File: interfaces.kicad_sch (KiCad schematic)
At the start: 23 parts, among them J3 SI-51005-F

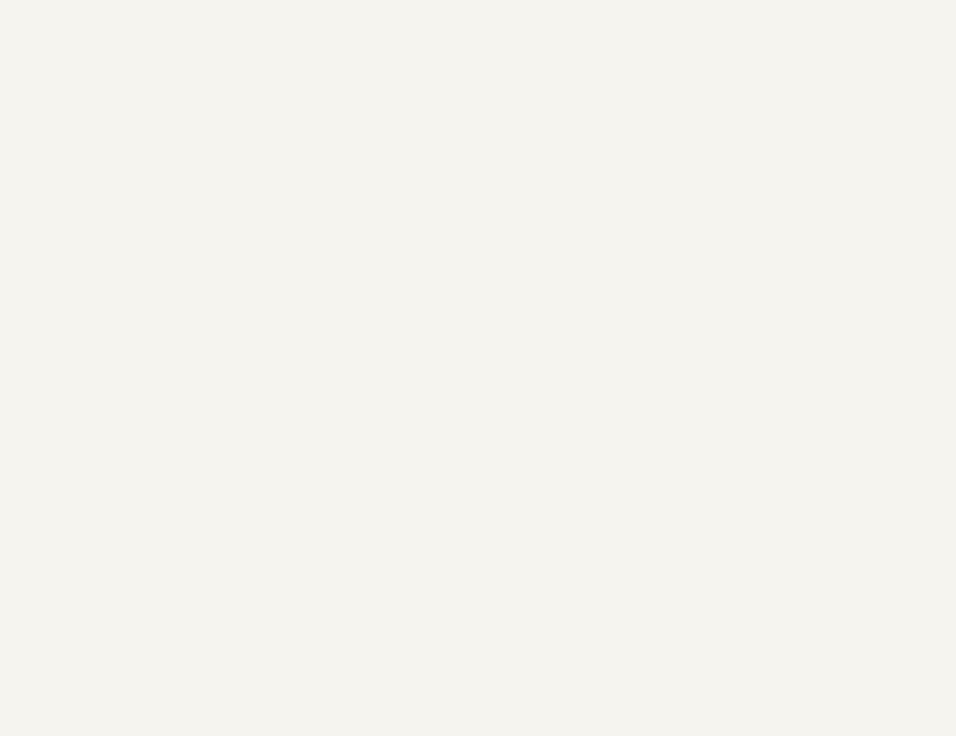
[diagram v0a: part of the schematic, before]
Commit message: Added I2C connector
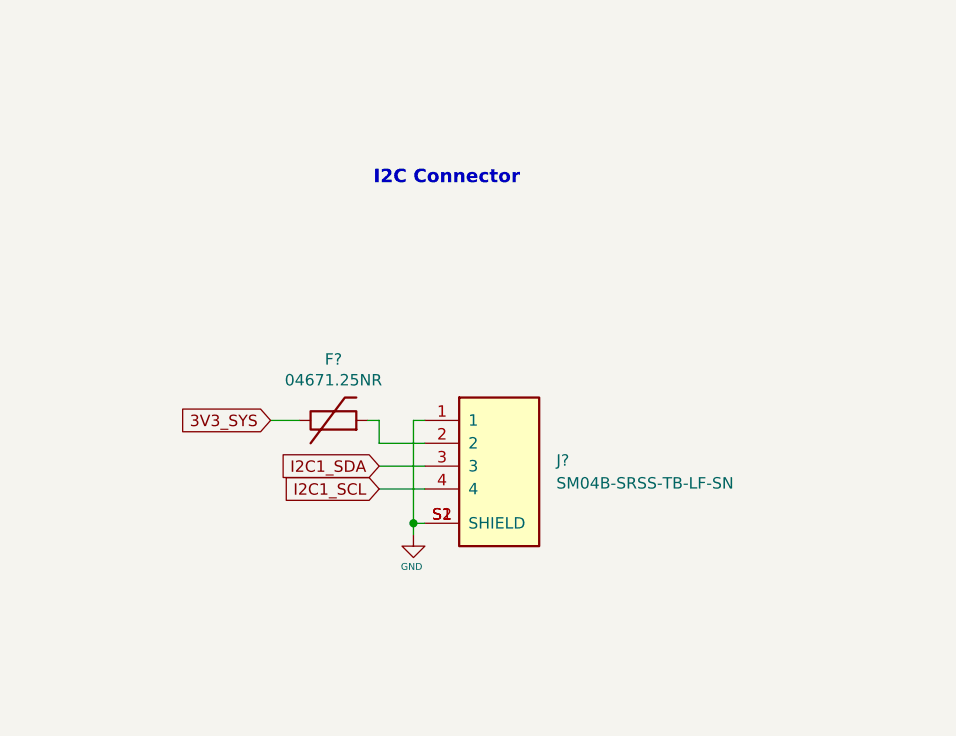
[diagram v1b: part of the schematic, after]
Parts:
- added F?: 04671.25NR, jetson-nano-baseboard-footprints:0603-Fuse-Littelfuse-0467, symbol jetson-nano-baseboard:04671.25NR
- added J?: SM04B-SRSS-TB-LF-SN, jetson-nano-baseboard-footprints:SM04B-SRSS-TB-LF-SN, symbol jetson-nano-baseboard:SM04B-SRSS-TB-LF-SN
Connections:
- net 3V3_SYS: now also F?.1
- net GND: now also J?.1, J?.S1 (SHIELD), J?.S2 (SHIELD)
- new net: F?.2, J?.2
- new net I2C1_SCL: J?.4
- new net I2C1_SDA: J?.3
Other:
- note added: "I2C Connector"
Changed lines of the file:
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@@
   (junction (at 161.925 142.24) (diameter 0) (color 0 0 0 0)
   )
+  (junction (at 305.435 76.2) (diameter 0) (color 0 0 0 0)
+  )
   (junction (at 113.665 129.54) (diameter 0) (color 0 0 0 0)
   )
@@
     (stroke (width 0) (type default) (color 0 0 0 0))
   )
+  (wire (pts (xy 300.355 64.77) (xy 301.625 64.77))
+    (stroke (width 0) (type default) (color 0 0 0 0))
+  )
   (wire (pts (xy 159.385 203.2) (xy 161.925 203.2))
     (stroke (width 0) (type default) (color 0 0 0 0))
@@
     (stroke (width 0) (type default) (color 0 0 0 0))
   )
+  (wire (pts (xy 305.435 76.2) (xy 306.705 76.2))
+    (stroke (width 0) (type default) (color 0 0 0 0))
+  )
   (wire (pts (xy 159.385 172.72) (xy 161.925 172.72))
     (stroke (width 0) (type default) (color 0 0 0 0))
@@
     (stroke (width 0) (type default) (color 0 0 0 0))
   )
+  (wire (pts (xy 305.435 77.47) (xy 305.435 76.2))
+    (stroke (width 0) (type default) (color 0 0 0 0))
+  )
   (wire (pts (xy 91.44 120.65) (xy 91.44 131.445))
     (stroke (width 0) (type default) (color 0 0 0 0))
@@
     (stroke (width 0) (type default) (color 0 0 0 0))
   )
+  (wire (pts (xy 301.625 64.77) (xy 301.625 67.31))
+    (stroke (width 0) (type default) (color 0 0 0 0))
+  )
   (wire (pts (xy 300.355 172.72) (xy 299.085 172.72))
     (stroke (width 0) (type default) (color 0 0 0 0))
@@
     (stroke (width 0) (type default) (color 0 0 0 0))
   )
+  (wire (pts (xy 301.625 72.39) (xy 306.705 72.39))
+    (stroke (width 0) (type default) (color 0 0 0 0))
+  )
   (wire (pts (xy 90.805 184.15) (xy 90.805 182.88))
     (stroke (width 0) (type default) (color 0 0 0 0))
@@
     (stroke (width 0) (type default) (color 0 0 0 0))
   )
+  (wire (pts (xy 301.625 69.85) (xy 306.705 69.85))
+    (stroke (width 0) (type default) (color 0 0 0 0))
+  )
   (wire (pts (xy 159.385 210.82) (xy 161.925 210.82))
     (stroke (width 0) (type default) (color 0 0 0 0))
@@
     (stroke (width 0) (type default) (color 0 0 0 0))
   )
+  (wire (pts (xy 289.56 64.77) (xy 292.735 64.77))
+    (stroke (width 0) (type default) (color 0 0 0 0))
+  )
+  (wire (pts (xy 305.435 64.77) (xy 305.435 76.2))
+    (stroke (width 0) (type default) (color 0 0 0 0))
+  )
   (wire (pts (xy 161.925 203.2) (xy 161.925 210.82))
     (stroke (width 0) (type default) (color 0 0 0 0))
@@
     (stroke (width 0) (type default) (color 0 0 0 0))
   )
+  (wire (pts (xy 301.625 67.31) (xy 306.705 67.31))
+    (stroke (width 0) (type default) (color 0 0 0 0))
+  )
   (wire (pts (xy 113.665 129.54) (xy 113.665 193.04))
     (stroke (width 0) (type default) (color 0 0 0 0))
   )
+  (wire (pts (xy 306.705 64.77) (xy 305.435 64.77))
+    (stroke (width 0) (type default) (color 0 0 0 0))
+  )
   (wire (pts (xy 161.925 218.44) (xy 161.925 229.235))
     (stroke (width 0) (type default) (color 0 0 0 0))
@@
     (effects (font (size 1.524 1.524)) (justify left bottom))
   )
+  (text "I2C Connector" (at 300.99 38.735 0)
+    (effects (font (size 1.4986 1.4986) (thickness 0.2997) bold) (justify left bottom))
+  )
   (text "Text" (at 67.7926 1253.8202 0)
     (effects (font (size 1.524 1.524)) (justify left bottom))
@@
     )
   )
+  (global_label "3V3_SYS" (shape input) (at 289.56 64.77 180) (fields_autoplaced)
+    (effects (font (size 1.27 1.27)) (justify right))
+    (property "Intersheet References" "${INTERSHEET_REFS}" (id 0) (at 168.91 145.415 0)
+      (effects (font (size 1.27 1.27)) hide)
+    )
+  )
   (global_label "PCIE0_TX0_P" (shape input) (at 212.09 152.4 0) (fields_autoplaced)
     (effects (font (size 1.27 1.27)) (justify left))
@@
     )
   )
+  (global_label "I2C1_SCL" (shape input) (at 301.625 72.39 180) (fields_autoplaced)
+    (effects (font (size 1.27 1.27)) (justify right))
+    (property "Intersheet References" "${INTERSHEET_REFS}" (id 0) (at 290.5318 72.3106 0)
+      (effects (font (size 1.27 1.27)) (justify right) hide)
+    )
+  )
   (global_label "1V8_SYS" (shape input) (at 101.6 120.65 90) (fields_autoplaced)
     (effects (font (size 1.27 1.27)) (justify left))
@@
     )
   )
+  (global_label "I2C1_SDA" (shape input) (at 301.625 69.85 180) (fields_autoplaced)
+    (effects (font (size 1.27 1.27)) (justify right))
+    (property "Intersheet References" "${INTERSHEET_REFS}" (id 0) (at 290.4713 69.7706 0)
+      (effects (font (size 1.27 1.27)) (justify right) hide)
+    )
+  )
   (global_label "PCIE0_RX1_P" (shape input) (at 212.09 175.26 0) (fields_autoplaced)
     (effects (font (size 1.27 1.27)) (justify left))
@@
     (pin "1")
     (pin "2")
+  )
+  (symbol (lib_id "jetson-nano-baseboard:SM04B-SRSS-TB-LF-SN") (at 311.785 71.12 0) (unit 1)
+    (in_bom yes) (on_board yes) (fields_autoplaced)
+    (property "Reference" "J?" (id 0) (at 321.31 69.2149 0)
+      (effects (font (size 1.27 1.27)) (justify left))
+    )
+    (property "Value" "SM04B-SRSS-TB-LF-SN" (id 1) (at 321.31 71.7549 0)
+      (effects (font (size 1.27 1.27)) (justify left))
+    )
+    (property "Footprint" "jetson-nano-baseboard-footprints:SM04B-SRSS-TB-LF-SN" (id 2) (at 311.785 85.09 0)
+      (effects (font (size 1.27 1.27)) hide)
+    )
+    (property "Datasheet" "https://www.jst-mfg.com/product/pdf/eng/eSH.pdf" (id 3) (at 300.355 86.36 0)
+      (effects (font (size 1.27 1.27)) hide)
+    )
+    (property "MPN" "SM04B-SRSS-TB-LF-SN" (id 4) (at 309.245 87.63 0)
+      (effects (font (size 1.27 1.27)) (justify left) hide)
+    )
+    (property "Manufacturer" "JST" (id 5) (at 309.245 90.17 0)
+      (effects (font (size 1.27 1.27)) (justify left) hide)
+    )
+    (pin "1")
+    (pin "2")
+    (pin "3")
+    (pin "4")
+    (pin "S1")
+    (pin "S2")
+  )
+  (symbol (lib_id "jetson-nano-baseboard:GND") (at 305.435 77.47 0) (unit 1)
+    (in_bom yes) (on_board yes)
+    (property "Reference" "#GND_?" (id 0) (at 305.435 77.47 0)
+      (effects (font (size 0.508 0.508)) hide)
+    )
+    (property "Value" "GND" (id 1) (at 305.2318 81.026 0)
+      (effects (font (size 0.762 0.762)))
+    )
+    (property "Footprint" "" (id 2) (at 305.435 77.47 0)
+      (effects (font (size 1.778 1.778)) hide)
+    )
+    (property "Datasheet" "" (id 3) (at 305.435 77.47 0)
+      (effects (font (size 1.778 1.778)) hide)
+    )
+    (pin "1")
+  )
+  (symbol (lib_id "jetson-nano-baseboard:04671.25NR") (at 296.545 64.77 0) (unit 1)
+    (in_bom yes) (on_board yes)
+    (property "Reference" "F?" (id 0) (at 296.545 57.9882 0))
+    (property "Value" "04671.25NR" (id 1) (at 296.545 60.2996 0))
+    (property "Footprint" "jetson-nano-baseboard-footprints:0603-Fuse-Littelfuse-0467" (id 2) (at 297.815 70.485 0)
+      (effects (font (size 1.27 1.27)) hide)
+    )
+    (property "Datasheet" "https://www.littelfuse.com/~/media/electronics/datasheets/fuses/littelfuse_fuse_467_datasheet.pdf.pdf" (id 3) (at 296.545 68.58 0)
+      (effects (font (size 1.27 1.27)) hide)
+    )
+    (property "MPN" "04671.25NR" (id 4) (at 297.18 72.39 0)
+      (effects (font (size 1.27 1.27)) hide)
+    )
+    (property "Manufacturer" "Littelfuse Inc." (id 5) (at 297.815 74.295 0)
+      (effects (font (size 1.27 1.27)) hide)
+    )
+    (pin "1")
+    (pin "2")

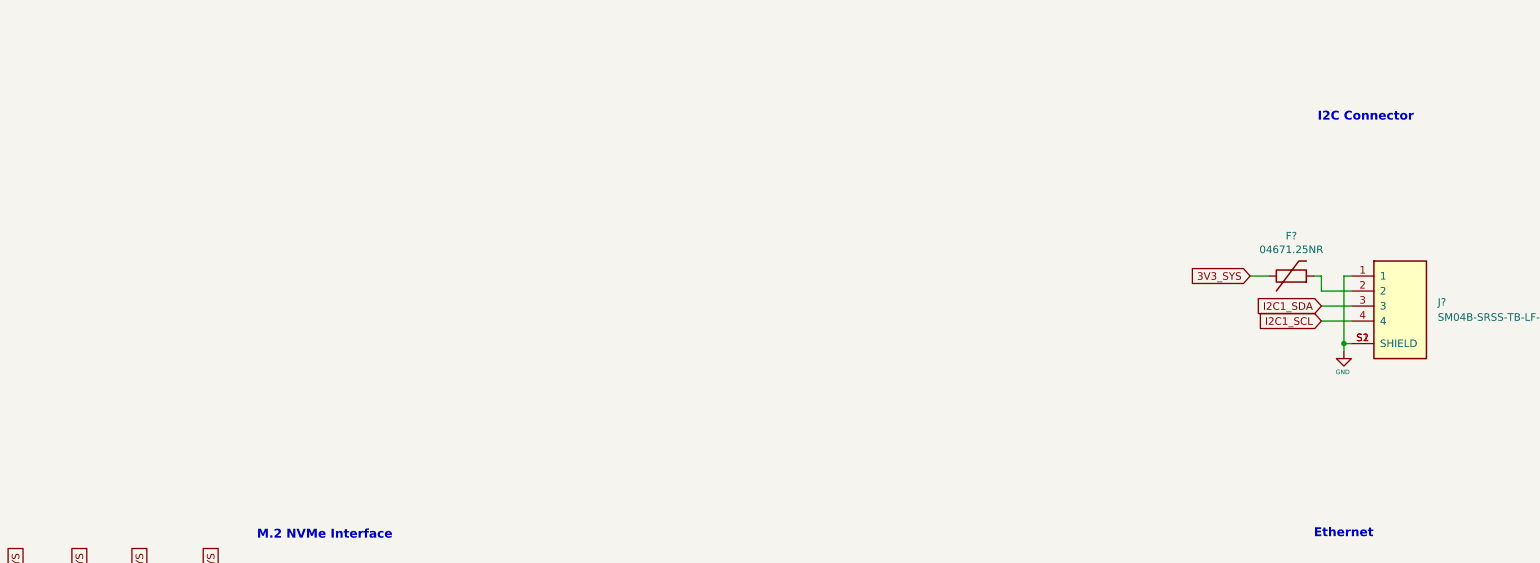
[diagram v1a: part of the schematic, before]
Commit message: Added CAN interface
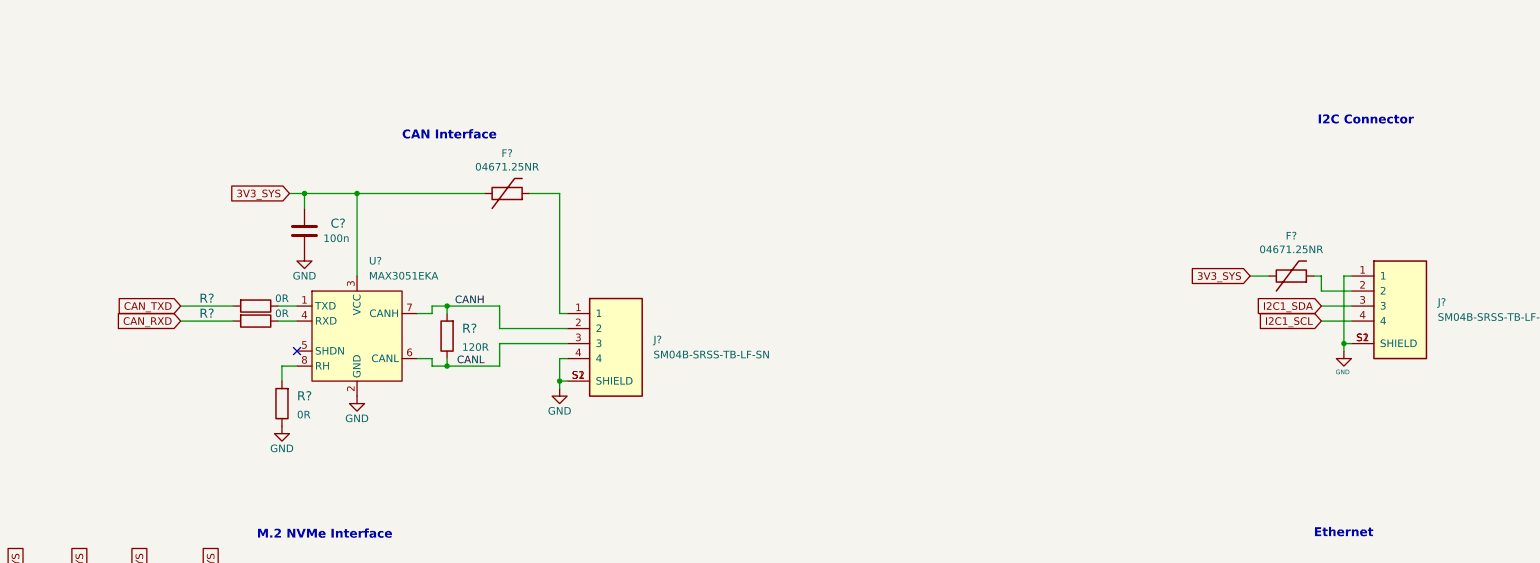
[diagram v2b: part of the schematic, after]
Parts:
- added C?: C_100n_0402, jetson-nano-baseboard-footprints:0402-cap, symbol jetson-nano-baseboard:C_100n_0402
- added F?: 04671.25NR, jetson-nano-baseboard-footprints:0603-Fuse-Littelfuse-0467, symbol jetson-nano-baseboard:04671.25NR
- added J?: SM04B-SRSS-TB-LF-SN, jetson-nano-baseboard-footprints:SM04B-SRSS-TB-LF-SN, symbol jetson-nano-baseboard:SM04B-SRSS-TB-LF-SN
- added R?: R_120R_0402, jetson-nano-baseboard-footprints:0402-res, symbol jetson-nano-baseboard:R_120R_0402
- added R? (x3): R_0R_0402, jetson-nano-baseboard-footprints:0402-res, symbol jetson-nano-baseboard:R_0R_0402
- added U?: MAX3051EKA, jetson-nano-baseboard-footprints:SOT-23-8, symbol jetson-nano-baseboard:MAX3051EKA
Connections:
- net 3V3_SYS: now also C?.2, F?.1, U?.3 (VCC)
- net GND: now also C?.1, J?.4, J?.S1 (SHIELD), J?.S2 (SHIELD), R?.1, U?.2 (GND)
- new net: F?.2, J?.1
- new net: R?.1, U?.1 (TXD)
- new net: R?.2, U?.8 (RH)
- new net: R?.1, U?.4 (RXD)
- new net CANH: J?.2, R?.2, U?.7 (CANH)
- new net CANL: J?.3, R?.1, U?.6 (CANL)
- new net CAN_RXD: R?.2
- new net CAN_TXD: R?.2
- no-connect marks 19 -> 20
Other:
- note added: "CAN Interface"
